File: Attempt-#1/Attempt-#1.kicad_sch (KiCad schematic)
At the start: 9 parts, among them U1 RP2040

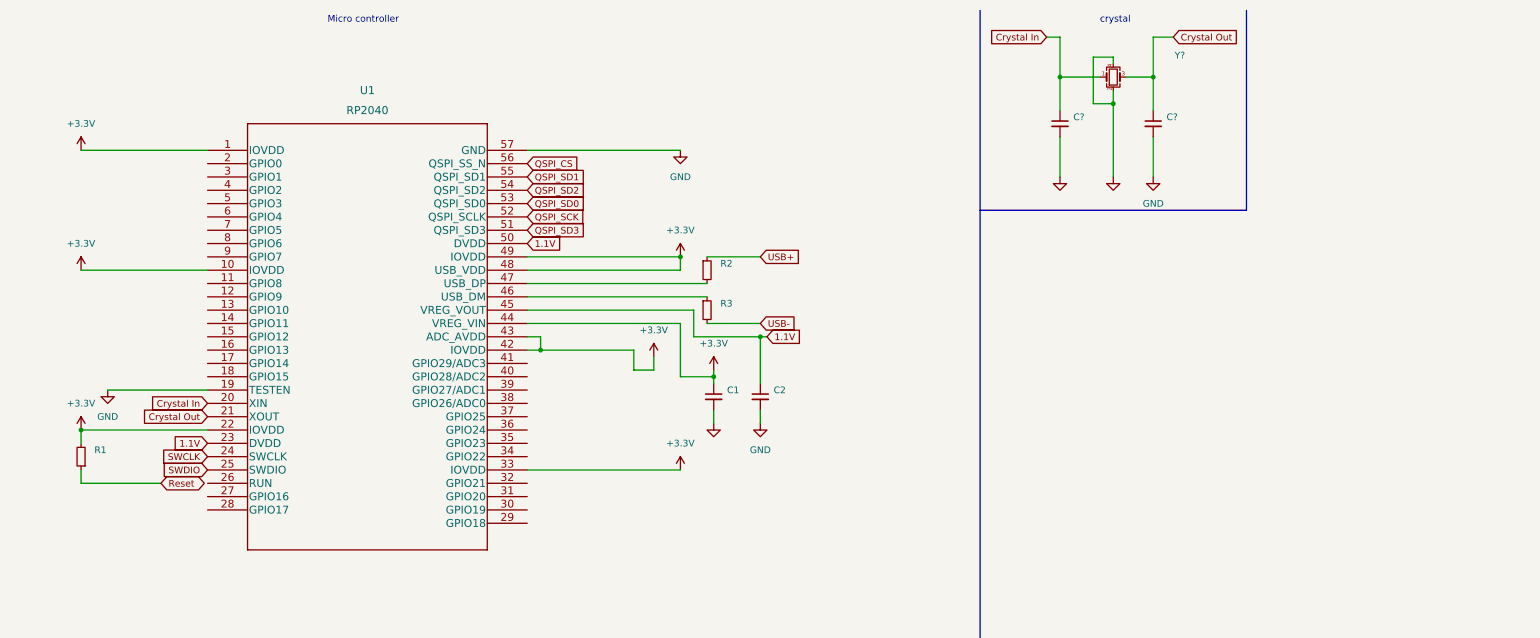
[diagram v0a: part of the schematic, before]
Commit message: Created circuitry for any power supplies going to MCU
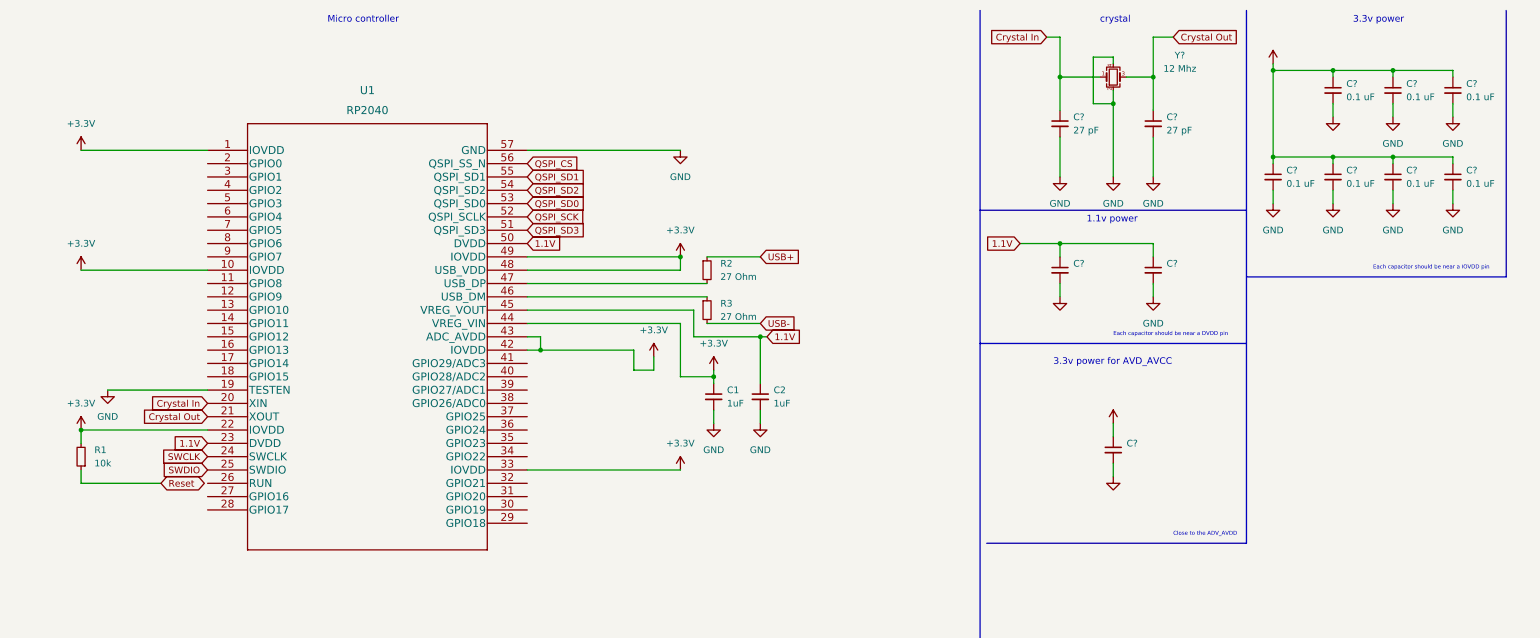
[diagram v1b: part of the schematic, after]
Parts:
- added C? (x7): 0.1 uF, symbol Device:C_Small
- added C? (x3): (no value), symbol Device:C_Small
- C1, C2: value (none) -> 1uF
- C? (x2): value (none) -> 27 pF
- R1: value (none) -> 10k
- R2, R3: value (none) -> 27 Ohm
- Y?: value (none) -> 12 Mhz
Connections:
- net +3V3: now also C?.1, C?.1, C?.1, C?.1, C?.1, C?.1, C?.1, C?.1
- net 1.1V: now also C?.1, C?.1
- net GND: now also C?.2, C?.2, C?.2, C?.2, C?.2, C?.2, C?.2, C?.2, C?.2, C?.2
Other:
- note added: "1.1v power"
- note added: "3.3v power"
- note added: "3.3v power for AVD_AVCC"
- note added: "Close to the ADV_AVDD"
- note added: "Each capacitor should be near a DVDD pin"
- note added: "Each capacitor should be near a IOVDD pin"

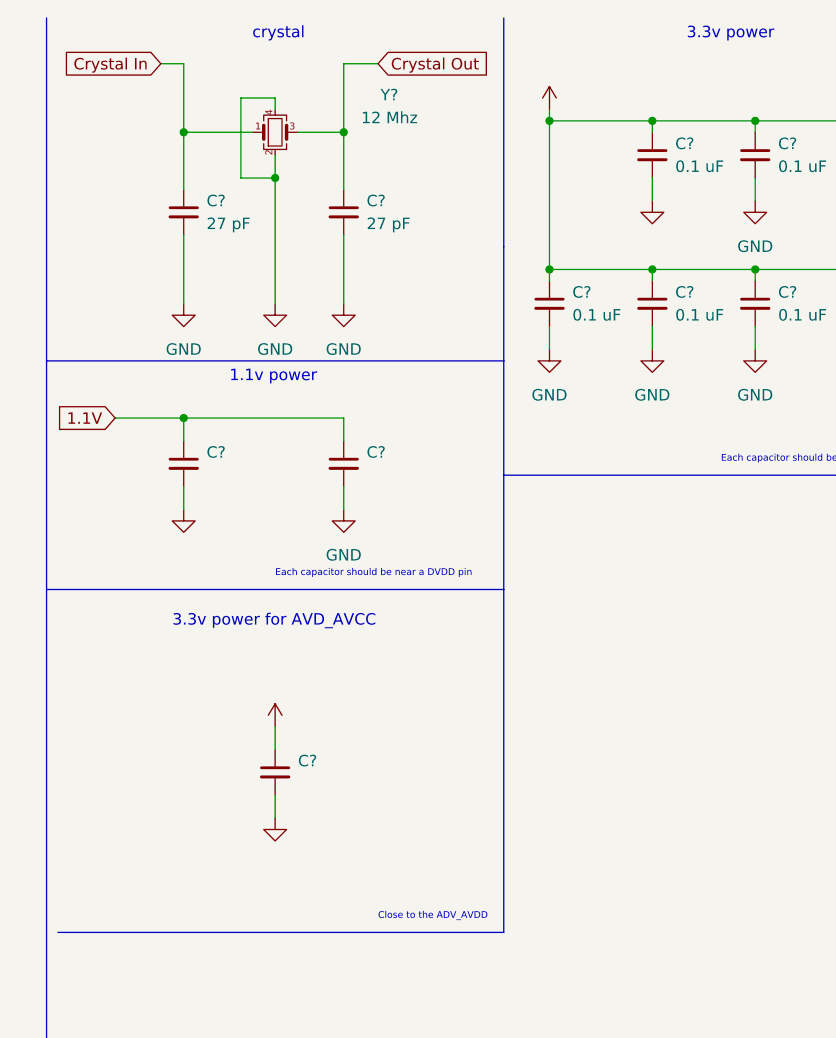
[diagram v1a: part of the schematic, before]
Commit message: Parts list and PDF created
Also created the power supply for DVDD pins.
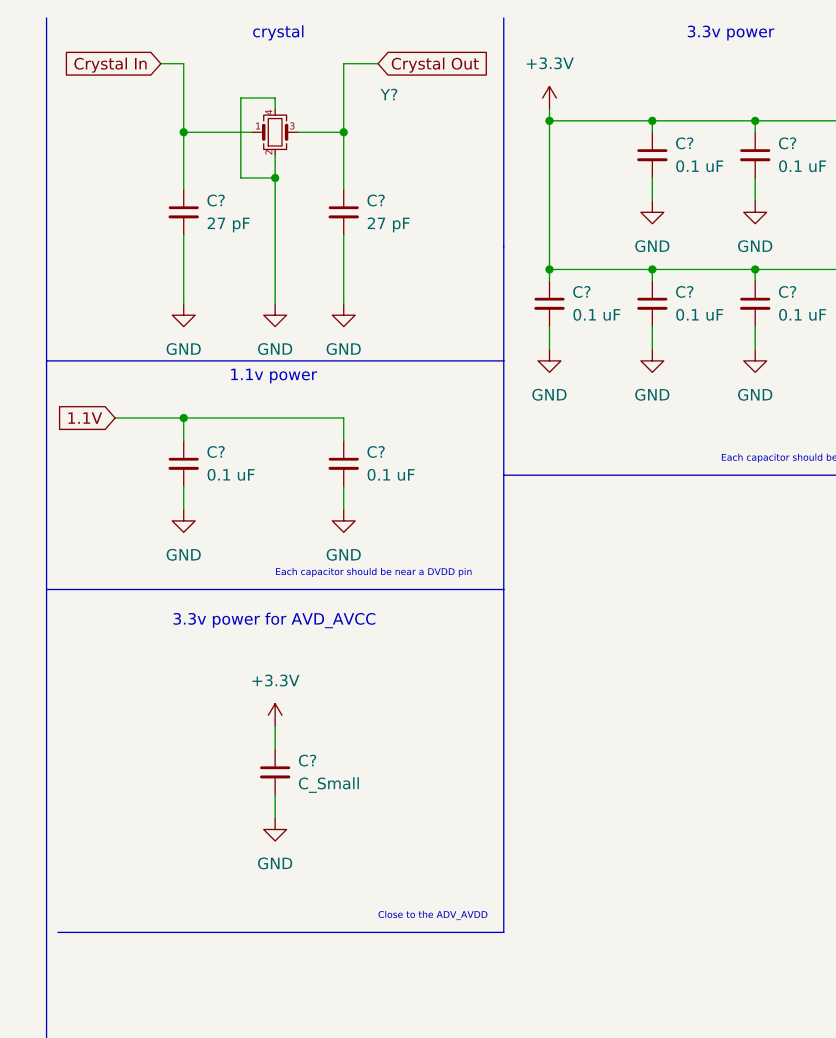
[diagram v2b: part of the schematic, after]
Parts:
- C? (x2): value (none) -> 0.1 uF
- C?: value (none) -> C_Small
- Y?: value 12 Mhz -> (none)
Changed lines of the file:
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@@
       (effects (font (size 1.27 1.27)) hide)
     )
-    (property "Value" "" (id 1) (at 224.79 72.39 0))
+    (property "Value" "GND" (id 1) (at 224.79 72.39 0))
     (property "Footprint" "" (id 2) (at 224.79 67.31 0)
       (effects (font (size 1.27 1.27)) hide)
@@
       (effects (font (size 1.27 1.27)) hide)
     )
-    (property "Value" "" (id 1) (at 276.86 38.1 0))
+    (property "Value" "GND" (id 1) (at 276.86 38.1 0))
     (property "Footprint" "" (id 2) (at 276.86 33.02 0)
       (effects (font (size 1.27 1.27)) hide)
@@
       (effects (font (size 1.27 1.27)) (justify left))
     )
-    (property "Value" "" (id 1) (at 227.33 63.5062 0)
+    (property "Value" "0.1 uF" (id 1) (at 227.33 63.5062 0)
       (effects (font (size 1.27 1.27)) (justify left))
     )
@@
       (effects (font (size 1.27 1.27)) hide)
     )
-    (property "Value" "" (id 1) (at 234.95 86.36 0))
+    (property "Value" "+3.3V" (id 1) (at 234.95 86.36 0))
     (property "Footprint" "" (id 2) (at 234.95 91.44 0)
       (effects (font (size 1.27 1.27)) hide)
@@
       (effects (font (size 1.27 1.27)) (justify left))
     )
-    (property "Value" "" (id 1) (at 237.49 97.7962 0)
+    (property "Value" "C_Small" (id 1) (at 237.49 97.7962 0)
       (effects (font (size 1.27 1.27)) (justify left))
     )
@@
       (effects (font (size 1.27 1.27)) hide)
     )
-    (property "Value" "" (id 1) (at 265.43 17.78 0))
+    (property "Value" "+3.3V" (id 1) (at 265.43 17.78 0))
     (property "Footprint" "" (id 2) (at 265.43 22.86 0)
       (effects (font (size 1.27 1.27)) hide)
@@
       (effects (font (size 1.27 1.27)) (justify left))
     )
-    (property "Value" "" (id 1) (at 245.11 63.5062 0)
+    (property "Value" "0.1 uF" (id 1) (at 245.11 63.5062 0)
       (effects (font (size 1.27 1.27)) (justify left))
     )
@@
       (effects (font (size 1.27 1.27)) hide)
     )
-    (property "Value" "" (id 1) (at 234.95 106.68 0))
+    (property "Value" "GND" (id 1) (at 234.95 106.68 0))
     (property "Footprint" "" (id 2) (at 234.95 101.6 0)
       (effects (font (size 1.27 1.27)) hide)
@@
     (in_bom yes) (on_board yes) (fields_autoplaced)
     (property "Reference" "Y?" (id 0) (at 247.65 21.2598 0))
-    (property "Value" "12 Mhz" (id 1) (at 247.65 23.7998 0))
+    (property "Value" "" (id 1) (at 247.65 23.7998 0))
     (property "Footprint" "" (id 2) (at 234.95 25.4 0)
       (effects (font (size 1.27 1.27)) hide)
     )
-    (property "Datasheet" "~" (id 3) (at 234.95 25.4 0)
-      (effects (font (size 1.27 1.27)) hide)
-    )
+    (property "Datasheet" "" (id 3) (at 234.95 25.4 0)
+      (effects (font (size 1.27 1.27)) hide)
+    )

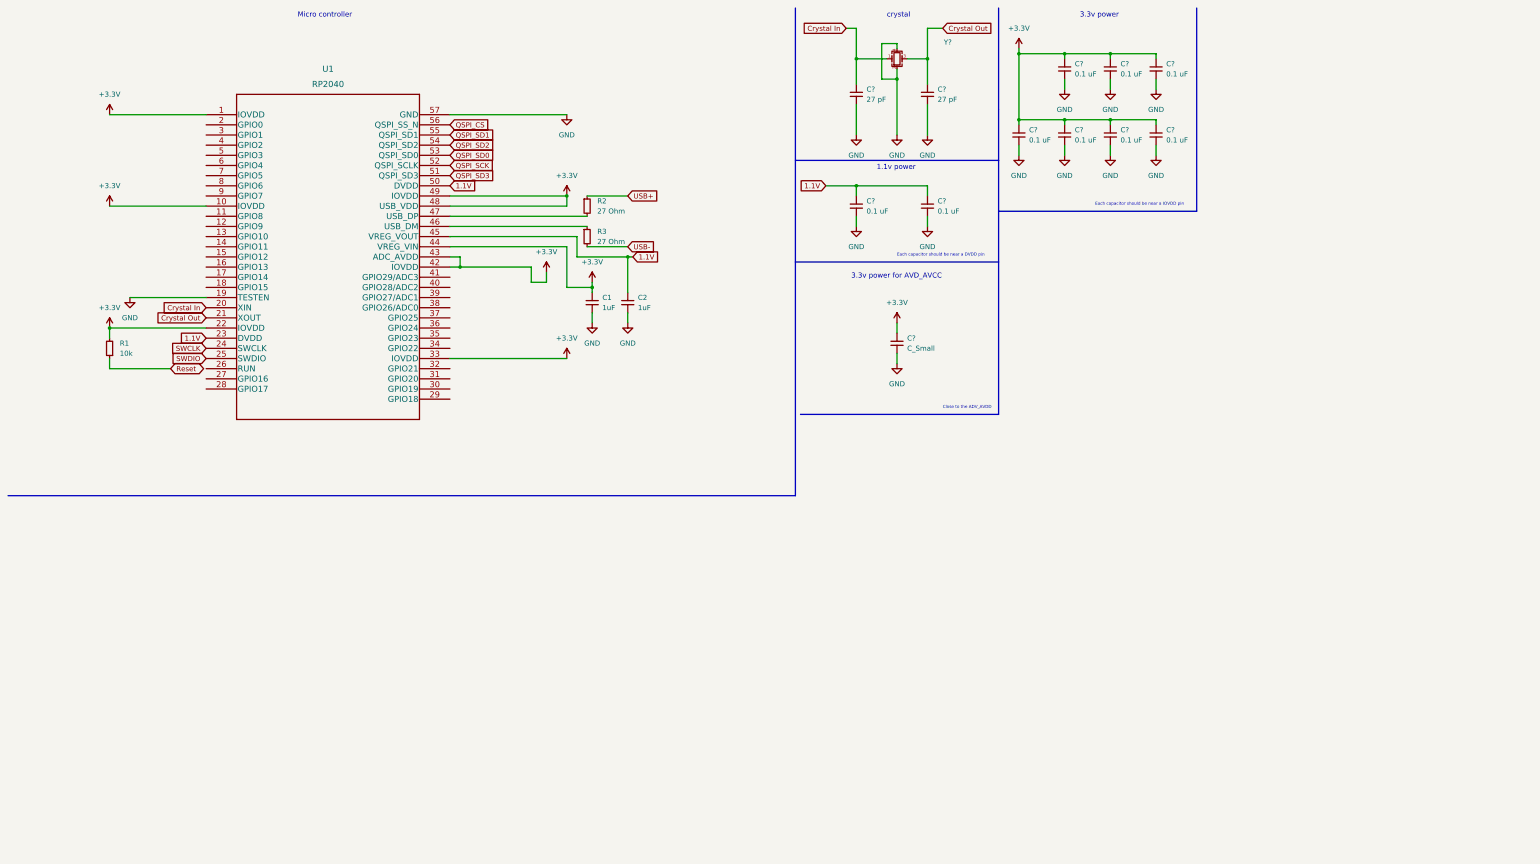
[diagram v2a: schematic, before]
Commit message: Added QSPI and some connectors
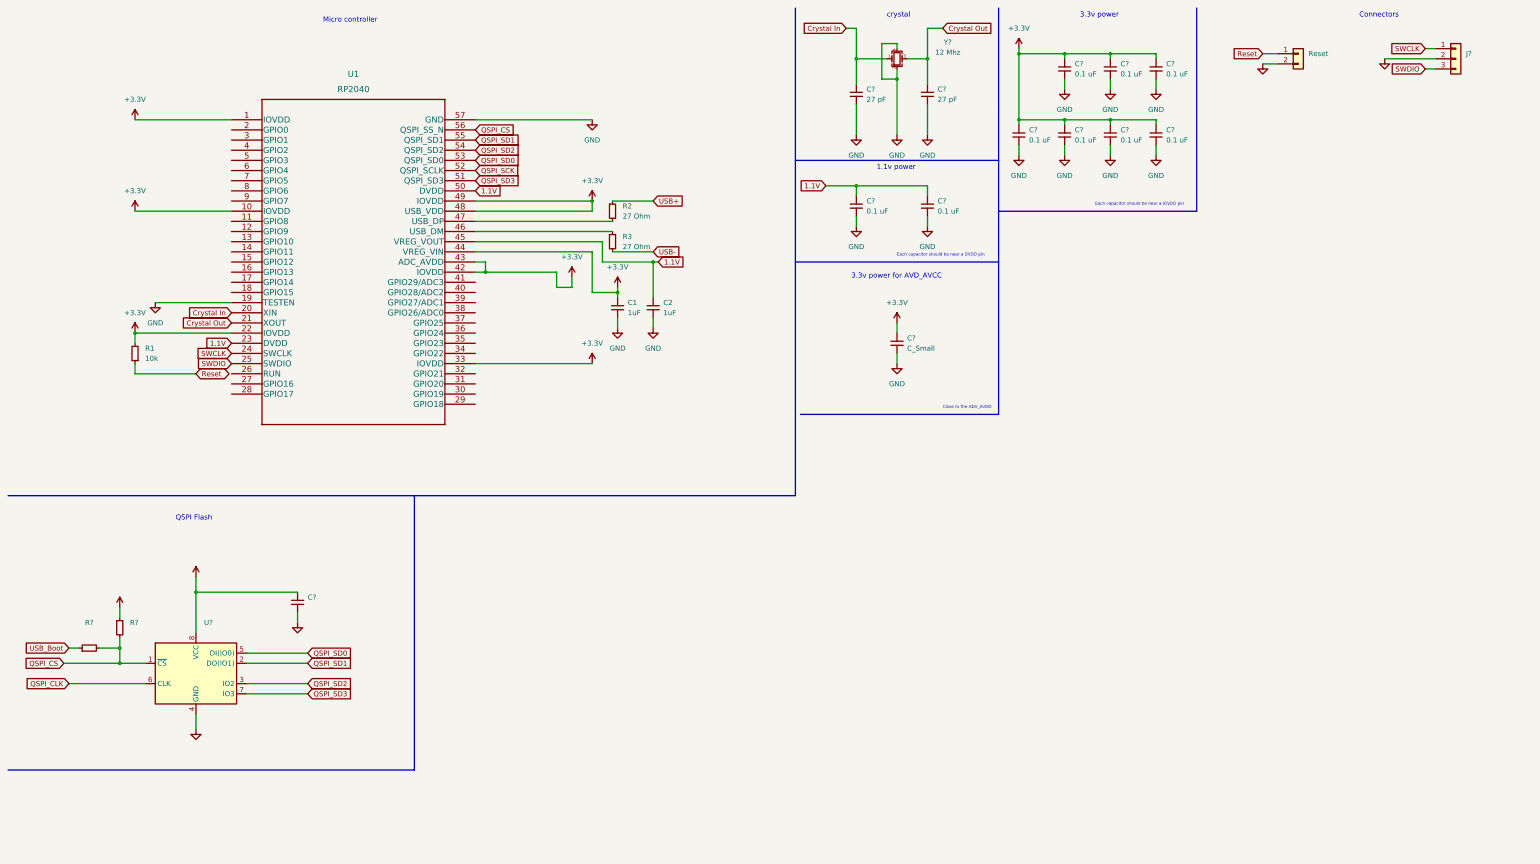
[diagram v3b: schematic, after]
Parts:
- added C?: (no value), symbol Device:C_Small
- added J?: (no value), symbol Connector_Generic:Conn_01x03
- added R? (x2): (no value), symbol Device:R_Small
- added Reset: (no value), symbol Connector_Generic:Conn_01x02
- added U?: (no value), symbol Memory_Flash:W25Q32JVSS
- Y?: value (none) -> 12 Mhz
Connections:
- net +3V3: now also C?.1, R?.1, U?.8 (VCC)
- net GND: now also C?.2, J?.2 (Pin_2), Reset.2 (Pin_2), U?.4 (GND)
- net QSPI_CS: now also R?.2, R?.2, U?.1 (~{CS})
- net QSPI_SD0: now also U?.5 (DI(IO0))
- net QSPI_SD1: now also U?.2 (DO(IO1))
- net QSPI_SD2: now also U?.3 (IO2)
- net QSPI_SD3: now also U?.7 (IO3)
- net Reset: now also Reset.1 (Pin_1)
- net SWCLK: now also J?.1 (Pin_1)
- net SWDIO: now also J?.3 (Pin_3)
- new net QSPI_CLK: U?.6 (CLK)
- new net USB_Boot: R?.1
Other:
- note added: "Connectors"
- note added: "QSPI Flash"
- company: (none) -> Diren Gomez
- title: (none) -> PCB Attempt 1
- moved on the sheet: C1, C2, R1, R2, R3, U1

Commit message: Started work on the USB C schematic
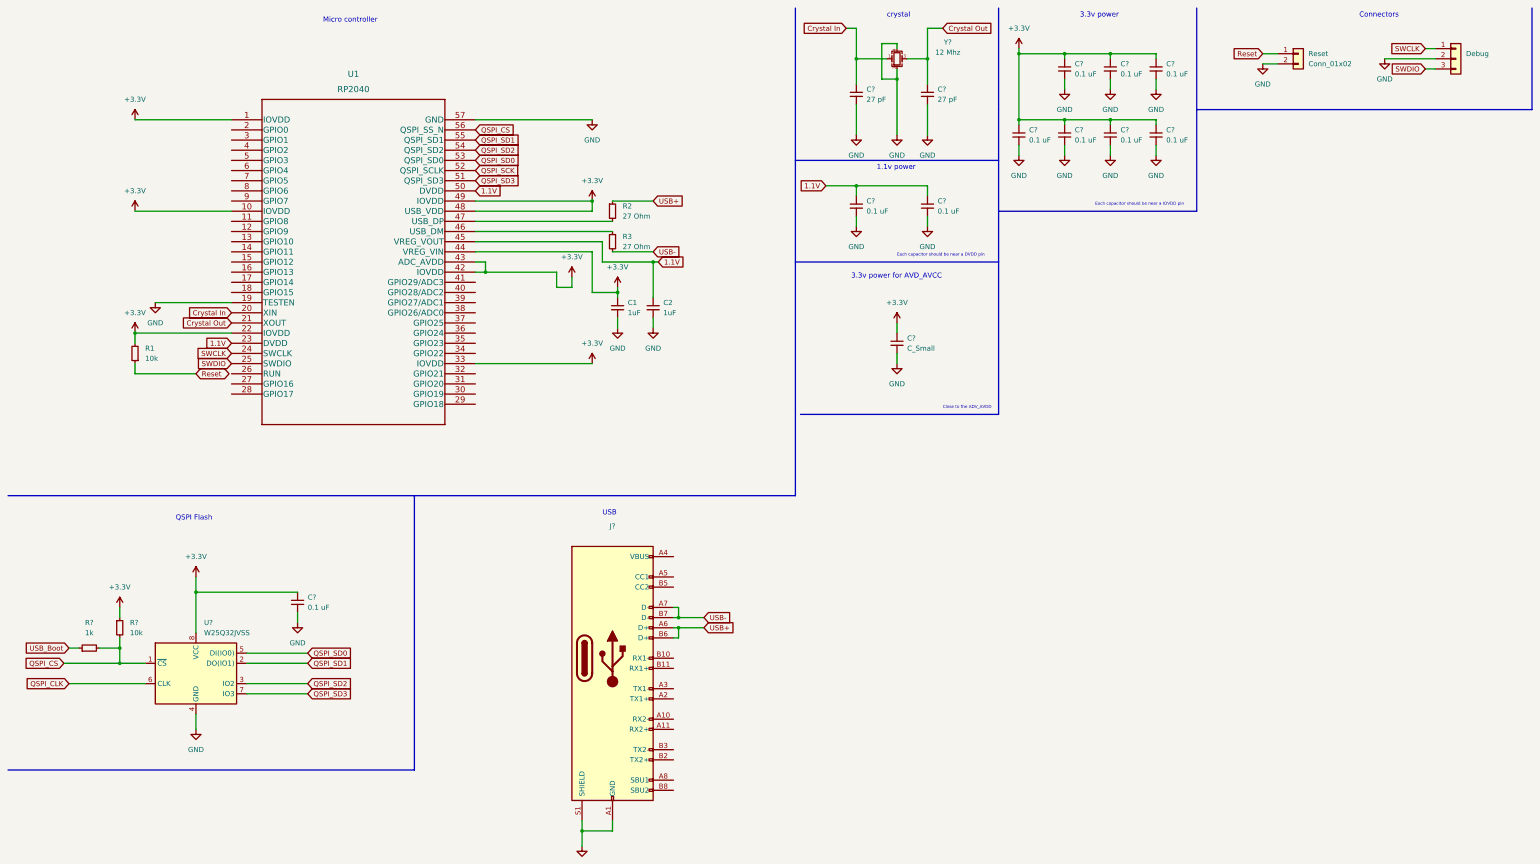
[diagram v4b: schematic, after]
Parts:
- added J?: (no value), symbol Connector:USB_C_Receptacle
- C?: value (none) -> 0.1 uF
- R?: value (none) -> 1k
- R?: value (none) -> 10k
- Reset: value (none) -> Conn_01x02
- U?: value (none) -> W25Q32JVSS; footprint (none) -> Package_SO:SOIC-8_5.23x5.23mm_P1.27mm
- gave numbers to parts that had none: 1
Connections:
- net GND: now also J?.A1 (GND), J?.A12 (GND), J?.B1 (GND), J?.B12 (GND), J?.S1 (SHIELD)
- net USB+: now also J?.A6 (D+), J?.B6 (D+)
- net USB-: now also J?.A7 (D-), J?.B7 (D-)
- new net: J?.A4 (VBUS), J?.A9 (VBUS), J?.B4 (VBUS), J?.B9 (VBUS)
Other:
- note added: "USB"
